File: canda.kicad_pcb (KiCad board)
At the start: 2 copper layers, 93.8 x 39 mm, 47 parts, among them J1 2s_cortex-m-10-pin, J3 2x4 male header 2.54 mm, J4 Conn_header_01x04_THT_2.54mm, J5 Screw_Terminal_01x02, J6 Screw_Terminal_01x02, M1 Motor_Servo, Q1 BSS138, Q2 DMG2305UX-13, U1 TPS613222ADBZ, U2 TLV75533PDBVR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

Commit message: ff
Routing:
- net +3.3V: track 44.9 -> 47.5 mm
- net Net-(U4-PB14): track 11.7 -> 10.2 mm
- net Net-(J3-Pin_4): track 50.6 -> 51.2 mm
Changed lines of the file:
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@@
+	)
+	(segment
+		(start 198.25 115.65)
+		(end 199.2 116.6)
+		(width 0.2)
+		(layer "F.Cu")
+		(net 4)
 	)
 	(segment
@@
 	)
 	(segment
+		(start 189.75 106.95)
+		(end 188.9 106.1)
+		(width 0.2)
+		(layer "F.Cu")
+		(net 4)
+	)
+	(segment
 		(start 192.75 105.5375)
 		(end 192.0375 105.5375)
@@
 	)
 	(segment
-		(start 191.3375 106.9375)
-		(end 190.6 106.2)
-		(width 0.2)
-		(layer "F.Cu")
-		(net 4)
-	)
-	(segment
 		(start 206.9 101.6)
 		(end 207.1 101.4)
@@
 	)
 	(segment
-		(start 198.25 113.8625)
-		(end 198.25 115.35)
-		(width 0.2)
-		(layer "F.Cu")
-		(net 4)
-	)
-	(segment
 		(start 188.925 118.1)
 		(end 188.925 111.475)
@@
 	)
 	(segment
+		(start 191.3375 106.95)
+		(end 189.75 106.95)
+		(width 0.2)
+		(layer "F.Cu")
+		(net 4)
+	)
+	(segment
 		(start 168.79 122.41)
 		(end 168.3 122.9)
@@
 	)
 	(segment
-		(start 198.25 115.35)
-		(end 198.8 115.9)
-		(width 0.2)
-		(layer "F.Cu")
-		(net 4)
-	)
-	(segment
 		(start 209.5 104.1)
 		(end 209.5 103.3)
@@
 	)
 	(segment
+		(start 198.25 113.8625)
+		(end 198.25 115.65)
+		(width 0.2)
+		(layer "F.Cu")
+		(net 4)
+	)
+	(segment
 		(start 202.3 119.9)
 		(end 202.7 119.5)
@@
 	)
 	(segment
-		(start 191.3375 106.95)
-		(end 191.3375 106.9375)
-		(width 0.2)
-		(layer "F.Cu")
-		(net 4)
-	)
-	(segment
 		(start 187.4875 101.1)
 		(end 187.6 101.1)
@@
 	)
 	(via
-		(at 198.8 115.9)
+		(at 199.2 116.6)
 		(size 0.6)
 		(drill 0.3)
@@
 	)
 	(via
-		(at 190.6 106.2)
+		(at 188.9 106.1)
 		(size 0.6)
 		(drill 0.3)
@@
 	)
 	(segment
-		(start 198.89259 111.45)
-		(end 200.95 111.45)
-		(width 0.2)
-		(layer "F.Cu")
-		(net 43)
-	)
-	(segment
 		(start 200.95 111.45)
 		(end 201.3 111.1)
@@
 	)
 	(segment
-		(start 199.6625 111.45)
-		(end 198.89259 111.45)
+		(start 200.95 111.45)
+		(end 199.6625 111.45)
 		(width 0.2)
 		(layer "F.Cu")
@@
 	(segment
 		(start 196.7 113.9125)
-		(end 196.75 113.8625)
+		(end 196.7 117.1)
+		(width 0.2)
+		(layer "F.Cu")
+		(net 51)
+	)
+	(segment
+		(start 196.7 117.1)
+		(end 196.35 117.45)
+		(width 0.2)
+		(layer "F.Cu")
+		(net 51)
+	)
+	(segment
+		(start 196.75 113.8625)
+		(end 196.7 113.9125)
 		(width 0.2)
 		(layer "F.Cu")
@@
 	)
 	(segment
-		(start 196.7 117.1)
-		(end 196.7 113.9125)
-		(width 0.2)
-		(layer "F.Cu")
-		(net 51)
-	)
-	(segment
 		(start 158.29 103.275)
 		(end 159.4 104.385)
@@
 	)
 	(via
-		(at 196.7 117.1)
-		(size 0.6)
-		(drill 0.3)
-		(layers "F.Cu" "B.Cu")
-		(net 51)
-	)
-	(segment
-		(start 196.1 117.7)
-		(end 196.7 117.1)
-		(width 0.2)
-		(layer "B.Cu")
+		(at 196.35 117.45)
+		(size 0.6)
+		(drill 0.3)
+		(layers "F.Cu" "B.Cu")
 		(net 51)
 	)
@@
 	)
 	(segment
+		(start 196.1 117.7)
+		(end 196.35 117.45)
+		(width 0.2)
+		(layer "B.Cu")
+		(net 51)
+	)
+	(segment
+		(start 197.25 113.8625)
+		(end 197.25 116.25)
+		(width 0.2)
+		(layer "F.Cu")
+		(net 52)
+	)
+	(segment
 		(start 160.83 103.275)
 		(end 161.8 104.245)
@@
 	)
 	(segment
-		(start 197.3 113.9125)
-		(end 197.25 113.8625)
-		(width 0.2)
-		(layer "F.Cu")
-		(net 52)
-	)
-	(segment
 		(start 161.8 104.245)
 		(end 161.8 115.9)
@@
 	)
 	(segment
-		(start 197.3 115.5)
-		(end 197.3 113.9125)
+		(start 197.25 116.25)
+		(end 197.3 116.3)
 		(width 0.2)
 		(layer "F.Cu")
@@
 	)
 	(via
-		(at 197.3 115.5)
+		(at 197.3 116.3)
 		(size 0.6)
 		(drill 0.3)
@@
 	)
 	(segment
-		(start 162.15 116.25)
-		(end 196.55 116.25)
+		(start 161.8 115.9)
+		(end 162.2 116.3)
 		(width 0.2)
 		(layer "B.Cu")
@@
 	)
 	(segment
-		(start 161.8 115.9)
-		(end 162.15 116.25)
-		(width 0.2)
-		(layer "B.Cu")
-		(net 52)
-	)
-	(segment
-		(start 196.55 116.25)
-		(end 197.3 115.5)
-		(width 0.2)
-		(layer "B.Cu")
+		(start 162.2 116.3)
+		(end 197.3 116.3)
+		(width 0.2)
+		(layer "B.Cu")

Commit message: updates
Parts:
- removed Q2: DMG2305UX-13, Package_TO_SOT_SMD:SOT-23-3
- added Q3: DMG2305UX-13, Package_TO_SOT_SMD:SOT-23-3, F.Cu at (192.5, 130.8)
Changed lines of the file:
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@@
 	(net 54 "/5V en")
 	(net 55 "unconnected-(U4-PB3-Pad39)")
-	(net 56 "Net-(Q2-D)")
-	(net 57 "Net-(Q2-G)")
+	(net 56 "Net-(Q3-D)")
+	(net 57 "Net-(Q1-D)")
 	(footprint "2s_misc:SW_TH_Tactile_Omron_B3F-1052"
 		(layer "F.Cu")
@@
 		(tags "resistor")
 		(property "Reference" "R8"
-			(at 0 -1.65 360)
+			(at 0 -1.65 0)
 			(layer "F.SilkS")
 			(effects
@@
 		)
 		(property "Value" "10k_0805"
-			(at 0 1.65 360)
+			(at 0 1.65 0)
 			(layer "F.Fab")
 			(effects
@@
 		)
 		(fp_text user "${REFERENCE}"
-			(at 0 0 360)
+			(at 0 0 0)
 			(layer "F.Fab")
 			(effects
@@
 		(tags "THT terminal block MaiXu MX126-5.0-02P pitch 5mm size 10.5x7.8mm drill 1.3mm pad 2.8mm")
 		(property "Reference" "J6"
-			(at 9.15 -0.1675 360)
+			(at 9.15 -0.1675 0)
 			(layer "F.SilkS")
 			(effects
@@
 		(tags "SOT TO_SOT_SMD")
 		(property "Reference" "Q1"
-			(at -3.4 0.1 360)
+			(at -3.4 0.1 0)
 			(layer "F.SilkS")
 			(effects
@@
 		)
 		(property "Value" "BSS138"
-			(at 0 2.4 360)
+			(at 0 2.4 0)
 			(layer "F.Fab")
 			(effects
@@
 		)
 		(fp_text user "${REFERENCE}"
-			(at 0 0 360)
+			(at 0 0 0)
 			(layer "F.Fab")
 			(effects
@@
 			(layers "F.Cu" "F.Paste" "F.Mask")
 			(roundrect_rratio 0.25)
-			(net 57 "Net-(Q2-G)")
+			(net 57 "Net-(Q1-D)")
 			(pinfunction "D")
 			(pintype "bidirectional")
@@
 		(tags "resistor")
 		(property "Reference" "R9"
-			(at 0 -1.65 360)
+			(at 0 -1.65 0)
 			(layer "F.SilkS")
 			(effects
@@
 		)
 		(property "Value" "10k_0805"
-			(at 0 1.65 360)
+			(at 0 1.65 0)
 			(layer "F.Fab")
 			(effects
@@
 		)
 		(fp_text user "${REFERENCE}"
-			(at 0 0 360)
+			(at 0 0 0)
 			(layer "F.Fab")
 			(effects
@@
 		)
 		(fp_text user "${REFERENCE}"
-			(at 0 2.54 360)
+			(at 0 2.54 0)
 			(layer "F.Fab")
 			(effects
@@
 		(tags "capacitor")
 		(property "Reference" "C1"
-			(at -3.5 -0.1 360)
+			(at -3.5 -0.1 0)
 			(layer "F.SilkS")
 			(effects
@@
 		)
 		(property "Value" "4.7uF_1206_lowESR"
-			(at 0 1.85 360)
+			(at 0 1.85 0)
 			(layer "F.Fab")
 			(effects
@@
 		)
 		(fp_text user "${REFERENCE}"
-			(at 0 0 360)
+			(at 0 0 0)
 			(layer "F.Fab")
 			(effects
@@
 		(tags "inductor taiyo-yuden nr smd")
 		(property "Reference" "L1"
-			(at 4.7375 -1.075 360)
+			(at 4.7375 -1.075 0)
 			(layer "F.SilkS")
 			(effects
@@
 		)
 		(property "Value" "33uH"
-			(at 0 4.5 360)
+			(at 0 4.5 0)
 			(layer "F.Fab")
 			(effects
@@
 		)
 		(fp_text user "${REFERENCE}"
-			(at 0 0 360)
+			(at 0 0 0)
 			(layer "F.Fab")
 			(effects
@@
 		)
 		(fp_text user "${REFERENCE}"
-			(at 0 3.81 360)
+			(at 0 3.81 0)
 			(layer "F.Fab")
 			(effects
@@
 			(size 1.6 5.7)
 			(layers "F.Cu" "F.Paste" "F.Mask")
-			(net 56 "Net-(Q2-D)")
+			(net 56 "Net-(Q3-D)")
 			(pinfunction "1")
 			(pintype "power_in")
@@
 		)
 		(fp_text user "${REFERENCE}"
-			(at 0 0 360)
+			(at 0 0 0)
 			(layer "F.Fab")
 			(effects
@@
 		(tags "capacitor")
 		(property "Reference" "C2"
-			(at -3.5 2.4 360)
+			(at -3.5 2.4 0)
 			(layer "F.SilkS")
 			(effects
@@
 		)
 		(property "Value" "2.2uF_1206_25V"
-			(at 0 1.85 360)
+			(at 0 1.85 0)
 			(layer "F.Fab")
 			(effects
@@
 		)
 		(fp_text user "${REFERENCE}"
-			(at 0 0 360)
+			(at 0 0 0)
 			(layer "F.Fab")
 			(effects
@@
 	(footprint "Package_TO_SOT_SMD:SOT-23-3"
 		(layer "F.Cu")
-		(at 192.5 130.8)
+		(at 192.4625 130.8)
 		(descr "SOT, 3 Pin (https://www.jedec.org/sites/default/files/docs/Mo-178D.PDF inferred 3-pin variant), generated with kicad-footprint-generator ipc_gullwing_generator.py")
 		(tags "SOT TO_SOT_SMD")
-		(property "Reference" "Q2"
-			(at 0 2.6 360)
+		(property "Reference" "Q3"
+			(at 0 -2.4 0)
 			(layer "F.SilkS")
 			(effects
@@
 		)
 		(property "Value" "DMG2305UX-13"
-			(at 0 2.4 360)
+			(at 0 2.4 0)
 			(layer "F.Fab")
 			(effects
@@
 			)
 		)
-		(property "Field5" ""
-			(at 0 0 0)
-			(unlocked yes)
-			(layer "F.Fab")
-			(hide yes)
-			(effects
-				(font
-					(size 1 1)
-					(thickness 0.15)
-				)
-			)
-		)
-		(property "Sim.Type" ""
-			(at 0 0 0)
-			(unlocked yes)
-			(layer "F.Fab")
-			(hide yes)
-			(effects
-				(font
-					(size 1 1)
-					(thickness 0.15)
-				)
-			)
-		)
-		(property "Field13" ""
-			(at 0 0 0)
-			(unlocked yes)
-			(layer "F.Fab")
-			(hide yes)
-			(effects
-				(font
-					(size 1 1)
-					(thickness 0.15)
-				)
-			)
-		)
 		(property "JLCPCB ID" "C144153"
 			(at 0 0 0)
@@
 			)
 		)
-		(property "JCLPCB ID" ""
-			(at 0 0 0)
-			(unlocked yes)
-			(layer "F.Fab")
-			(hide yes)
-			(effects
-				(font
-					(size 1 1)
-					(thickness 0.15)
-				)
-			)
-		)
-		(property "JLCPCB" ""
-			(at 0 0 0)
-			(unlocked yes)
-			(layer "F.Fab")
-			(hide yes)
-			(effects
-				(font
-					(size 1 1)
-					(thickness 0.15)
-				)
-			)
-		)
-		(property "Sim.Device" ""
-			(at 0 0 0)
-			(unlocked yes)
-			(layer "F.Fab")
-			(hide yes)
-			(effects
-				(font
-					(size 1 1)
-					(thickness 0.15)
-				)
-			)
-		)
-		(property "Sim.Pins" ""
-			(at 0 0 0)
-			(unlocked yes)
-			(layer "F.Fab")
-			(hide yes)
-			(effects
-				(font
-					(size 1 1)
-					(thickness 0.15)
-				)
-			)
-		)
 		(sheetname "Root")
 		(sheetfile "canda.kicad_sch")
@@
 		)
 		(fp_text user "${REFERENCE}"
-			(at 0 0 360)
+			(at 0 0 0)
 			(layer "F.Fab")
 			(effects
@@
 			(layers "F.Cu" "F.Paste" "F.Mask")
 			(roundrect_rratio 0.25)
-			(net 57 "Net-(Q2-G)")
+			(net 57 "Net-(Q1-D)")
 			(pinfunction "G")
 			(pintype "bidirectional")
@@
 			(layers "F.Cu" "F.Paste" "F.Mask")
 			(roundrect_rratio 0.25)
-			(net 56 "Net-(Q2-D)")
+			(net 56 "Net-(Q3-D)")
 			(pinfunction "D")
 			(pintype "power_out")
@@
 			(layers "F.Cu" "F.Paste" "F.Mask")
 			(roundrect_rratio 0.217391)
-			(net 56 "Net-(Q2-D)")
+			(net 56 "Net-(Q3-D)")
 			(pintype "passive")
 		)
@@
 			(layers "F.Cu" "F.Paste" "F.Mask")
 			(roundrect_rratio 0.243902)
-			(net 57 "Net-(Q2-G)")
+			(net 57 "Net-(Q1-D)")
 			(pintype "passive")
 		)
@@
 		(tags "resistor")
 		(property "Reference" "R7"
-			(at -2.9 0 360)
+			(at -2.9 0 0)
 			(layer "F.SilkS")
 			(effects
@@
 		)
 		(property "Value" "10k_0805"
-			(at 0 1.65 360)
+			(at 0 1.65 0)
 			(layer "F.Fab")
 			(effects
@@
 		)
 		(fp_text user "${REFERENCE}"
-			(at 0 0 360)
+			(at 0 0 0)
 			(layer "F.Fab")
 			(effects

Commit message: ?
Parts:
- removed R11: 47k_0805, Resistor_SMD:R_0805_2012Metric
- added R13: 47k_0805, Resistor_SMD:R_0805_2012Metric, F.Cu at (192.0, 122.8)

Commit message: updates
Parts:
- H1, H2, H3, H4: footprint MountingHole:MountingHole_3.2mm_M3_ISO7380_Pad -> MountingHole:MountingHole_3.2mm_M3_ISO7380
- J6: footprint 2s_connectors:TerminalBlock_MaiXu_MX126-5.0-02P_1x02_P5.00mm -> TerminalBlock_MetzConnect:TerminalBlock_MetzConnect_Type094_RT03502HBLU_1x02_P5.00mm_Horizontal
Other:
- board text added: "Canda v1.0"
- board text added: "Emmy & Mirco"

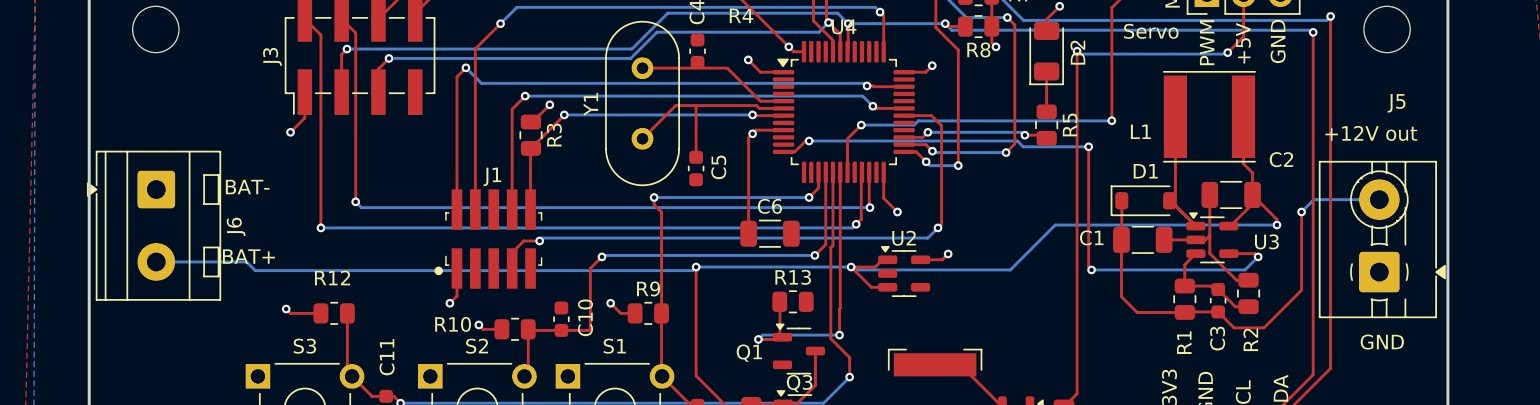
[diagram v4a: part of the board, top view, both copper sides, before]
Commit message: update terminal block
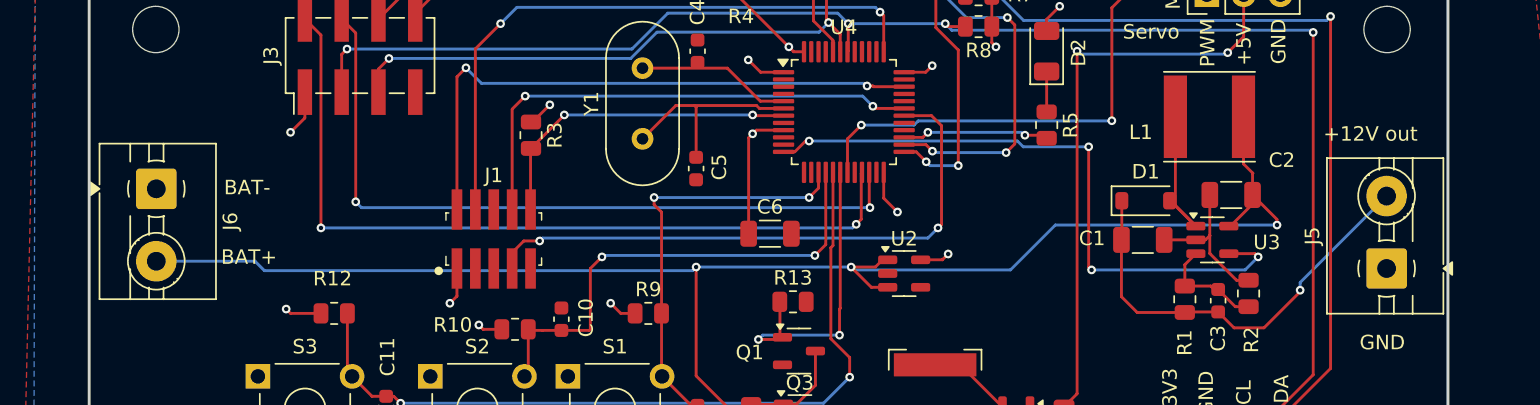
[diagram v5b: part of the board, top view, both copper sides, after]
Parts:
- J6: footprint TerminalBlock_MetzConnect:TerminalBlock_MetzConnect_Type094_RT03502HBLU_1x02_P5.00mm_Horizontal -> 2s_connectors:TerminalBlock_MaiXu_MX126-5.0-02P_1x02_P5.00mm
- moved J5 0.56 mm to (233.0, 120.5)
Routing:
- net +12V: track 32.2 -> 30.0 mm
- net GND: track 14.0 -> 15.2 mm
